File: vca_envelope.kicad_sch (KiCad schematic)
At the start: 19 parts, among them Q3 BC237, U11 4001, U12 4066, U13 Opamp_Dual

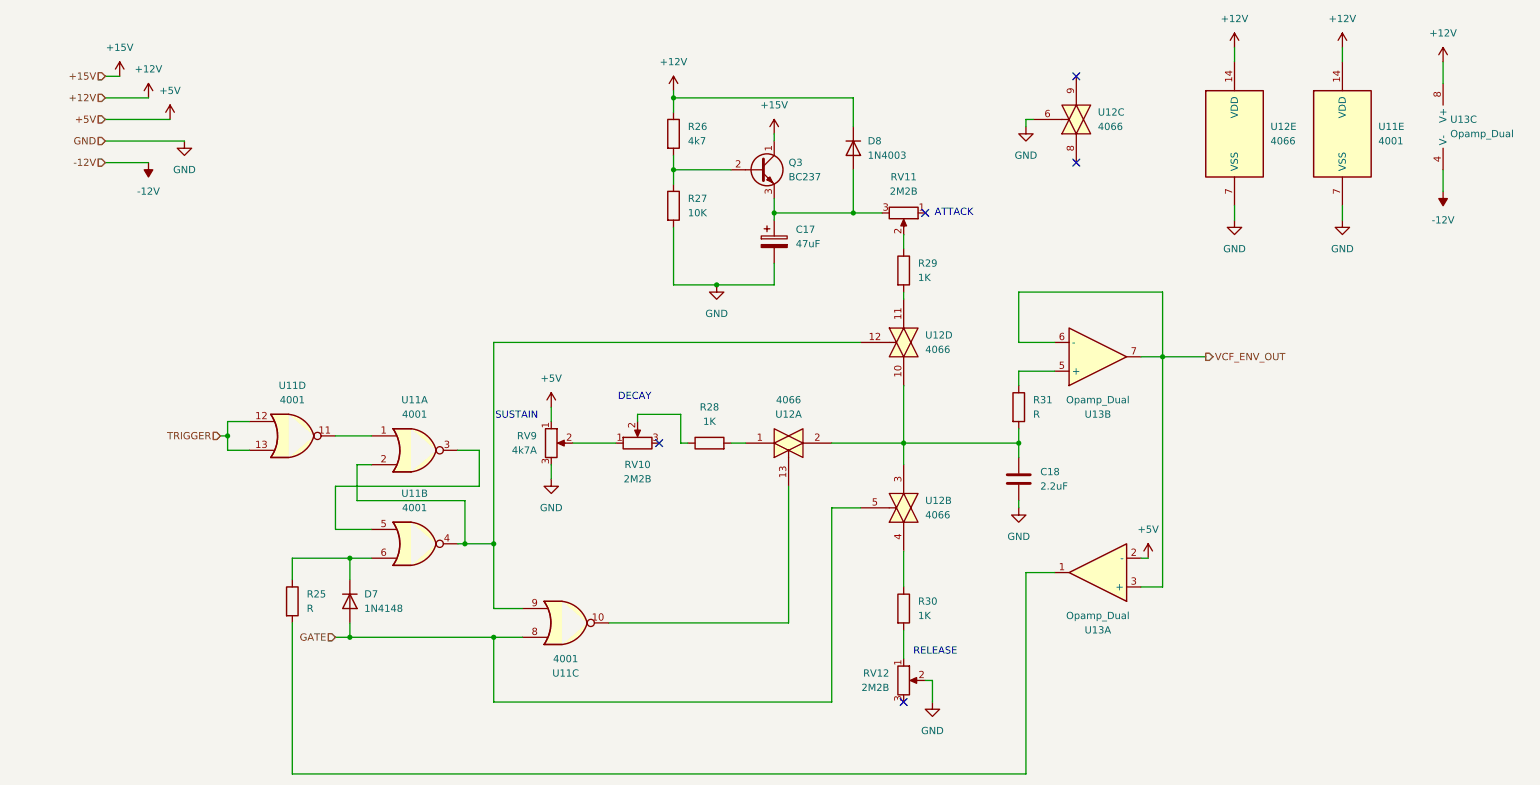
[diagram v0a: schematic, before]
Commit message: Add missing values and connectors
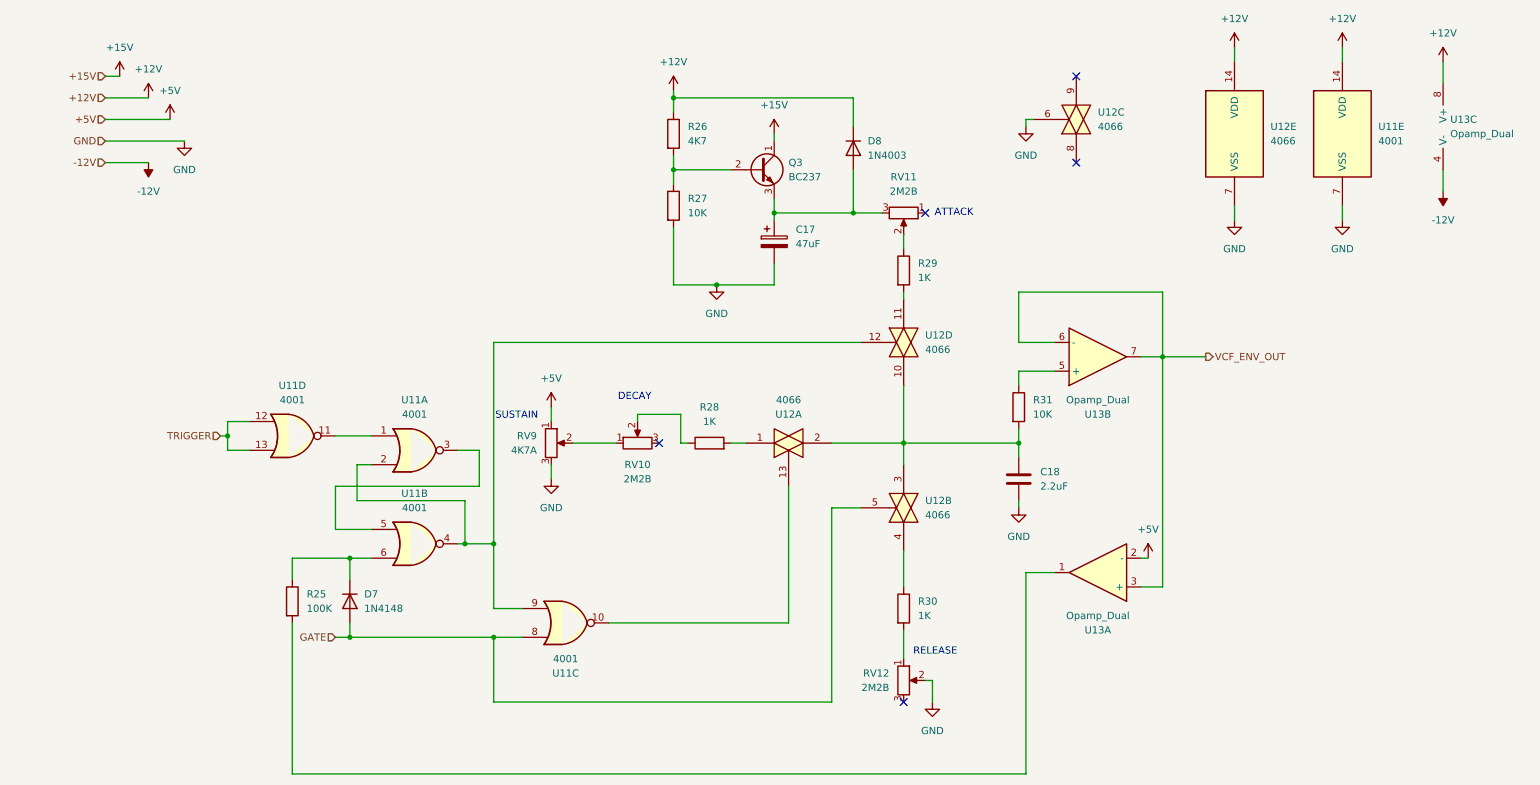
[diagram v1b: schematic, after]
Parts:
- R25: value R -> 100K
- R26: value 4k7 -> 4K7
- R31: value R -> 10K
- RV9: value 4k7A -> 4K7A
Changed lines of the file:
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@@
 			)
 		)
-		(property "Value" "4k7A"
+		(property "Value" "4K7A"
 			(at 106.68 100.3299 0)
 			(effects
@@
 			)
 		)
-		(property "Value" "R"
+		(property "Value" "10K"
 			(at 194.31 93.9799 0)
 			(effects
@@
 			)
 		)
-		(property "Value" "4k7"
+		(property "Value" "4K7"
 			(at 133.35 45.7199 0)
 			(effects
@@
 			)
 		)
-		(property "Value" "R"
+		(property "Value" "100K"
 			(at 66.04 128.2699 0)
 			(effects

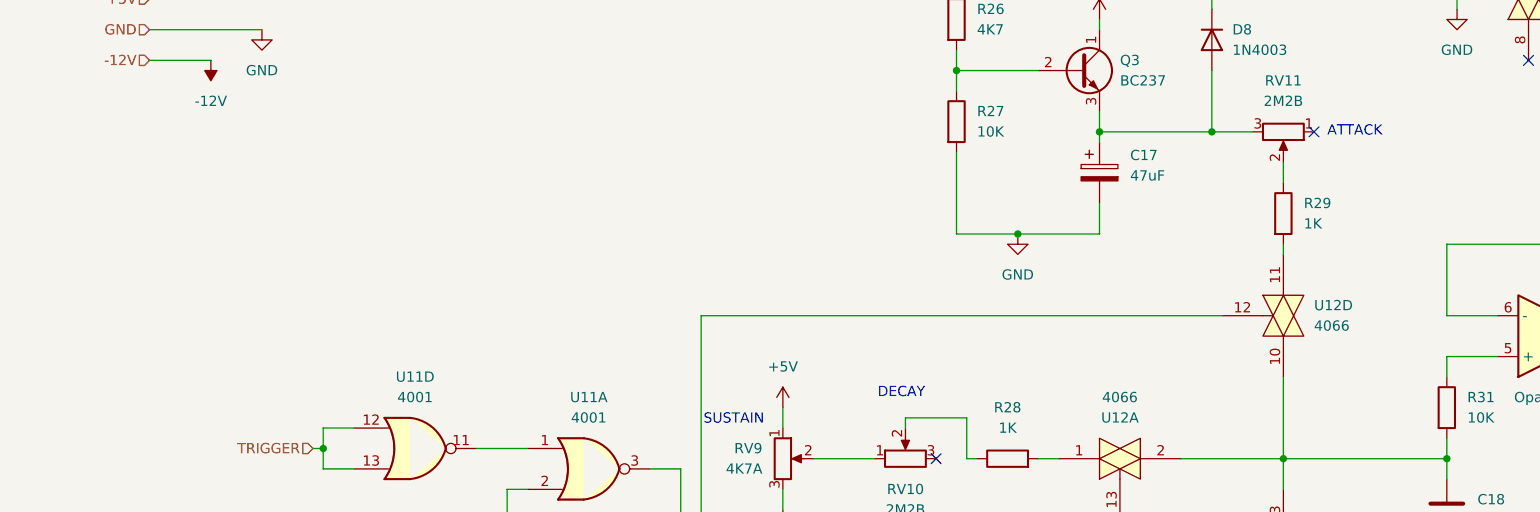
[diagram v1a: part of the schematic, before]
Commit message: Assign footprints and start PCB
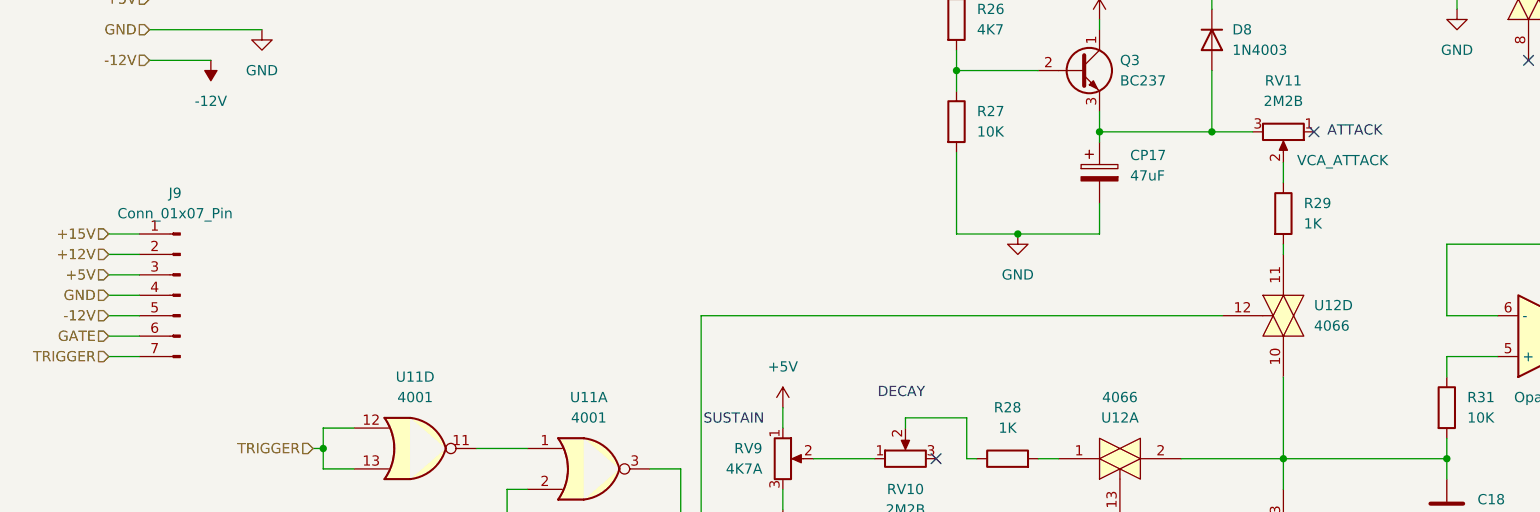
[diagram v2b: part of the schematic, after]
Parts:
- added J9: Conn_01x07_Pin, Connector_PinHeader_2.54mm:PinHeader_1x07_P2.54mm_Vertical, symbol Connector:Conn_01x07_Pin
- C18: footprint (none) -> Capacitor_THT:C_Disc_D5.0mm_W2.5mm_P5.00mm
- CP17: renamed from C17; footprint (none) -> Capacitor_THT:CP_Radial_D8.0mm_P3.80mm
- R25, R26, R27, R28, R29, R30, R31: footprint (none) -> Resistor_THT:R_Axial_DIN0204_L3.6mm_D1.6mm_P7.62mm_Horizontal
- RV10, RV11, RV12, RV9: footprint (none) -> Potentiometer_THT:Potentiometer_Omeg_PC16BU_Vertical
- U11: footprint (none) -> Package_DIP:DIP-16_W7.62mm_LongPads
- U12: footprint (none) -> Package_DIP:DIP-14_W7.62mm_LongPads
- U13: footprint (none) -> Package_DIP:DIP-8_W7.62mm_LongPads
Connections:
- net +12V: now also J9.2 (Pin_2)
- net +15V: now also J9.1 (Pin_1)
- net +5V: now also J9.3 (Pin_3)
- net -12V: now also J9.5 (Pin_5)
- net GATE: now also J9.6 (Pin_6)
- net GND: now also J9.4 (Pin_4)
- net TRIGGER: now also J9.7 (Pin_7)

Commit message: VCO components are in position
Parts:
- Q3: footprint Package_TO_SOT_THT:TO-92_Inline -> Package_TO_SOT_THT:TO-92_Inline_Wide
- R25, R26, R27, R28: footprint Resistor_THT:R_Axial_DIN0204_L3.6mm_D1.6mm_P7.62mm_Horizontal -> Resistor_THT:R_Axial_DIN0309_L9.0mm_D3.2mm_P12.70mm_Horizontal
- R29, R30, R31: footprint Resistor_THT:R_Axial_DIN0204_L3.6mm_D1.6mm_P7.62mm_Horizontal -> Resistor_THT:R_Axial_DIN0207_L6.3mm_D2.5mm_P15.24mm_Horizontal
- U11: footprint Package_DIP:DIP-16_W7.62mm_LongPads -> Package_DIP:DIP-14_W7.62mm_Socket_LongPads
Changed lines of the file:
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@@
 			)
 		)
-		(property "Footprint" "Package_DIP:DIP-16_W7.62mm_LongPads"
+		(property "Footprint" "Package_DIP:DIP-14_W7.62mm_Socket_LongPads"
 			(at 63.5 97.79 0)
 			(effects
@@
 			)
 		)
-		(property "Footprint" "Package_TO_SOT_THT:TO-92_Inline"
+		(property "Footprint" "Package_TO_SOT_THT:TO-92_Inline_Wide"
 			(at 151.13 52.705 0)
 			(effects
@@
 			)
 		)
-		(property "Footprint" "Resistor_THT:R_Axial_DIN0204_L3.6mm_D1.6mm_P7.62mm_Horizontal"
+		(property "Footprint" "Resistor_THT:R_Axial_DIN0207_L6.3mm_D2.5mm_P15.24mm_Horizontal"
 			(at 169.672 128.27 90)
 			(effects
@@
 			)
 		)
-		(property "Footprint" "Resistor_THT:R_Axial_DIN0204_L3.6mm_D1.6mm_P7.62mm_Horizontal"
+		(property "Footprint" "Resistor_THT:R_Axial_DIN0309_L9.0mm_D3.2mm_P12.70mm_Horizontal"
 			(at 137.16 100.838 90)
 			(effects
@@
 			)
 		)
-		(property "Footprint" "Resistor_THT:R_Axial_DIN0204_L3.6mm_D1.6mm_P7.62mm_Horizontal"
+		(property "Footprint" "Resistor_THT:R_Axial_DIN0207_L6.3mm_D2.5mm_P15.24mm_Horizontal"
 			(at 169.672 68.58 90)
 			(effects
@@
 			)
 		)
-		(property "Footprint" "Resistor_THT:R_Axial_DIN0204_L3.6mm_D1.6mm_P7.62mm_Horizontal"
+		(property "Footprint" "Resistor_THT:R_Axial_DIN0207_L6.3mm_D2.5mm_P15.24mm_Horizontal"
 			(at 189.992 92.71 90)
 			(effects
@@
 			)
 		)
-		(property "Footprint" "Package_DIP:DIP-16_W7.62mm_LongPads"
+		(property "Footprint" "Package_DIP:DIP-14_W7.62mm_Socket_LongPads"
 			(at 85.09 116.84 0)
 			(effects
@@
 			)
 		)
-		(property "Footprint" "Package_DIP:DIP-16_W7.62mm_LongPads"
+		(property "Footprint" "Package_DIP:DIP-14_W7.62mm_Socket_LongPads"
 			(at 85.09 100.33 0)
 			(effects
@@
 			)
 		)
-		(property "Footprint" "Package_DIP:DIP-16_W7.62mm_LongPads"
+		(property "Footprint" "Package_DIP:DIP-14_W7.62mm_Socket_LongPads"
 			(at 111.76 130.81 0)
 			(effects
@@
 			)
 		)
-		(property "Footprint" "Resistor_THT:R_Axial_DIN0204_L3.6mm_D1.6mm_P7.62mm_Horizontal"
+		(property "Footprint" "Resistor_THT:R_Axial_DIN0309_L9.0mm_D3.2mm_P12.70mm_Horizontal"
 			(at 129.032 44.45 90)
 			(effects
@@
 			)
 		)
-		(property "Footprint" "Package_DIP:DIP-16_W7.62mm_LongPads"
+		(property "Footprint" "Package_DIP:DIP-14_W7.62mm_Socket_LongPads"
 			(at 248.92 44.45 0)
 			(effects
@@
 			)
 		)
-		(property "Footprint" "Resistor_THT:R_Axial_DIN0204_L3.6mm_D1.6mm_P7.62mm_Horizontal"
+		(property "Footprint" "Resistor_THT:R_Axial_DIN0309_L9.0mm_D3.2mm_P12.70mm_Horizontal"
 			(at 129.032 57.15 90)
 			(effects
@@
 			)
 		)
-		(property "Footprint" "Resistor_THT:R_Axial_DIN0204_L3.6mm_D1.6mm_P7.62mm_Horizontal"
+		(property "Footprint" "Resistor_THT:R_Axial_DIN0309_L9.0mm_D3.2mm_P12.70mm_Horizontal"
 			(at 61.722 127 90)
 			(effects

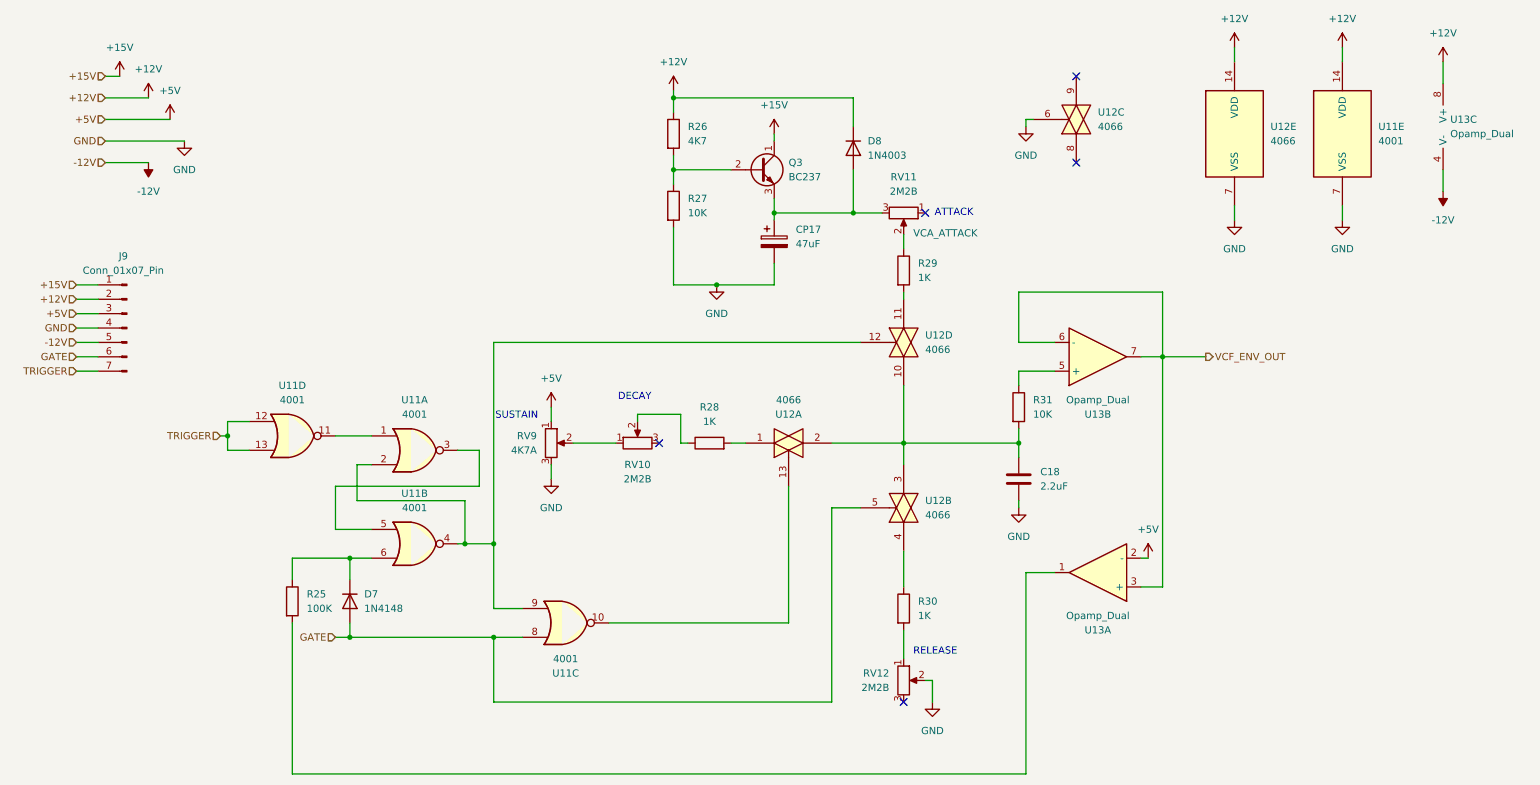
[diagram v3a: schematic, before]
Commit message: Fix PCB sizes, adjust layout to new size
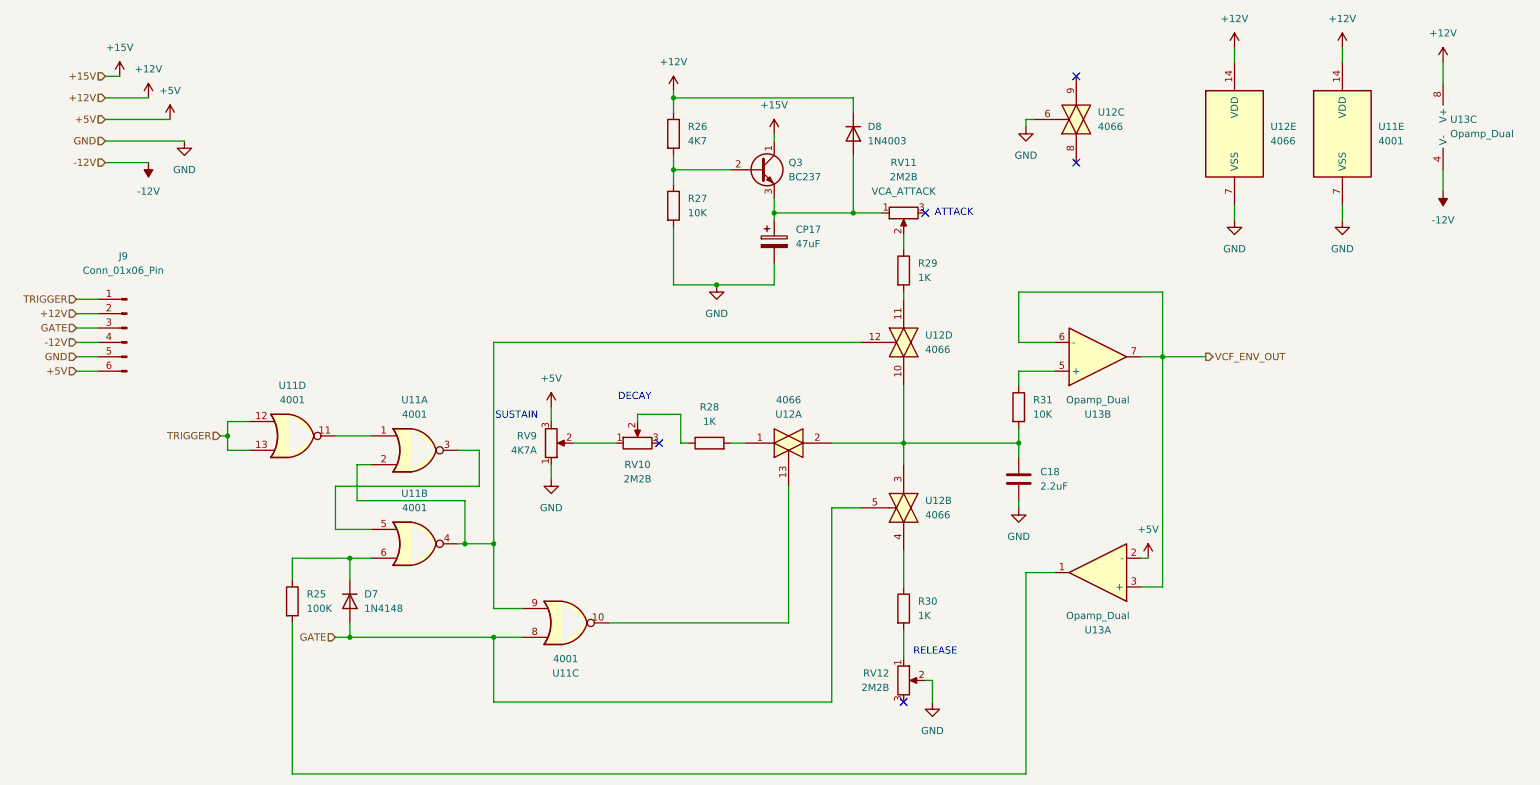
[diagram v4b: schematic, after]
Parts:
- J9: value Conn_01x07_Pin -> Conn_01x06_Pin; footprint Connector_PinHeader_2.54mm:PinHeader_1x07_P2.54mm_Vertical -> Connector_PinHeader_2.54mm:PinHeader_1x06_P2.54mm_Vertical; symbol Connector:Conn_01x07_Pin -> Connector:Conn_01x06_Pin
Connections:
- net +15V: no longer J9.1 (Pin_1)
- net +5V: now also J9.6 (Pin_6), RV9.3; no longer J9.3 (Pin_3), RV9.1
- net -12V: now also J9.4 (Pin_4); no longer J9.5 (Pin_5)
- net GATE: now also J9.3 (Pin_3); no longer J9.6 (Pin_6)
- net GND: now also J9.5 (Pin_5), RV9.1; no longer J9.4 (Pin_4), RV9.3
- net TRIGGER: now also J9.1 (Pin_1); no longer J9.7 (Pin_7)
- net at CP17.1, D8.2 (A), Q3.3 (E): now also RV11.1; no longer RV11.3
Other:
- moved on the sheet: D8, RV11
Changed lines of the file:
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@@
 	(wire
 		(pts
-			(xy 162.56 58.42) (xy 162.56 50.8)
+			(xy 162.56 58.42) (xy 162.56 48.26)
 		)
 		(stroke
@@
 	(wire
 		(pts
-			(xy 25.4 71.12) (xy 29.21 71.12)
-		)
-		(stroke
-			(width 0)
-			(type default)
-		)
-	)
-	(wire
-		(pts
 			(xy 167.64 58.42) (xy 162.56 58.42)
 		)
@@
 	(wire
 		(pts
-			(xy 162.56 43.18) (xy 162.56 38.1)
+			(xy 162.56 40.64) (xy 162.56 38.1)
 		)
 		(stroke
@@
 	(hierarchical_label "+5V"
 		(shape input)
-		(at 25.4 76.2 180)
+		(at 25.4 86.36 180)
 		(effects
 			(font
@@
 	(hierarchical_label "GND"
 		(shape input)
-		(at 25.4 78.74 180)
+		(at 25.4 83.82 180)
 		(effects
 			(font
@@
 		)
 	)
-	(hierarchical_label "+15V"
-		(shape input)
-		(at 25.4 71.12 180)
-		(effects
-			(font
-				(size 1.27 1.27)
-			)
-			(justify right)
-		)
-	)
 	(hierarchical_label "+5V"
 		(shape input)
@@
 	(hierarchical_label "GATE"
 		(shape input)
-		(at 25.4 83.82 180)
+		(at 25.4 78.74 180)
 		(effects
 			(font
@@
 	(hierarchical_label "+12V"
 		(shape input)
-		(at 25.4 73.66 180)
+		(at 25.4 76.2 180)
 		(effects
 			(font
@@
 	(hierarchical_label "TRIGGER"
 		(shape input)
-		(at 25.4 86.36 180)
+		(at 25.4 73.66 180)
 		(effects
 			(font
@@
 		(lib_id "Device:R_Potentiometer")
 		(at 109.22 99.06 0)
+		(mirror x)
 		(unit 1)
 		(exclude_from_sim no)
@@
 		(on_board yes)
 		(dnp no)
-		(fields_autoplaced yes)
 		(property "Reference" "RV12"
 			(at 168.91 139.6999 0)
@@
 	(symbol
 		(lib_id "Device:R_Potentiometer")
-		(at 171.45 58.42 270)
+		(at 171.45 58.42 90)
+		(mirror x)
 		(unit 1)
 		(exclude_from_sim no)
@@
 		(on_board yes)
 		(dnp no)
+		(fields_autoplaced yes)
 		(property "Reference" "RV11"
-			(at 171.45 52.07 90)
+			(at 171.45 49.53 90)
 			(effects
 				(font
@@
 		)
 		(property "Value" "2M2B"
-			(at 171.45 54.61 90)
+			(at 171.45 52.07 90)
 			(effects
 				(font
@@
 		)
 		(property "Description" "VCA_ATTACK"
-			(at 178.816 61.976 90)
+			(at 171.45 54.61 90)
 			(effects
 				(font
@@
 	(symbol
 		(lib_id "Diode:1N4003")
-		(at 162.56 46.99 270)
+		(at 162.56 44.45 270)
 		(unit 1)
 		(exclude_from_sim no)
@@
 		(fields_autoplaced yes)
 		(property "Reference" "D8"
-			(at 165.1 45.7199 90)
+			(at 165.1 43.1799 90)
 			(effects
 				(font
@@
 		)
 		(property "Value" "1N4003"
-			(at 165.1 48.2599 90)
+			(at 165.1 45.7199 90)
 			(effects
 				(font
@@
 		)
 		(property "Footprint" "Diode_THT:D_DO-41_SOD81_P10.16mm_Horizontal"
-			(at 158.115 46.99 0)
+			(at 158.115 44.45 0)
 			(effects
 				(font
@@
 		)
 		(property "Datasheet" "http://www.vishay.com/docs/88503/1n4001.pdf"
-			(at 162.56 46.99 0)
+			(at 162.56 44.45 0)
 			(effects
 				(font
@@
 		)
 		(property "Description" "200V 1A General Purpose Rectifier Diode, DO-41"
-			(at 162.56 46.99 0)
+			(at 162.56 44.45 0)
 			(effects
 				(font
@@
 		)
 		(property "Sim.Device" "D"
-			(at 162.56 46.99 0)
+			(at 162.56 44.45 0)
 			(effects
 				(font
@@
 		)
 		(property "Sim.Pins" "1=K 2=A"
-			(at 162.56 46.99 0)
+			(at 162.56 44.45 0)
 			(effects
 				(font
@@
 	)
 	(symbol
-		(lib_id "Connector:Conn_01x07_Pin")
+		(lib_id "Connector:Conn_01x06_Pin")
 		(at 34.29 78.74 0)
 		(mirror y)
@@
 			)
 		)
-		(property "Value" "Conn_01x07_Pin"
+		(property "Value" "Conn_01x06_Pin"
 			(at 33.655 68.58 0)
 			(effects
@@
 			)
 		)
-		(property "Footprint" "Connector_PinHeader_2.54mm:PinHeader_1x07_P2.54mm_Vertical"
+		(property "Footprint" "Connector_PinHeader_2.54mm:PinHeader_1x06_P2.54mm_Vertical"
 			(at 34.29 78.74 0)
 			(effects
@@
 			)
 		)
-		(property "Description" "Generic connector, single row, 01x07, script generated"
+		(property "Description" "Generic connector, single row, 01x06, script generated"
 			(at 34.29 78.74 0)
 			(effects
@@
 		(pin "6"
 		)
-		(pin "7"
-		)
 		(instances
